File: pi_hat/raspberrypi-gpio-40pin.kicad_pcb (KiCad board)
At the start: 2 copper layers, 65 x 56 mm, 86 parts, among them J1 MC000052, J2 10pinIDC, J3 MOLEX_2031, P1 Conn_02x20_Odd_Even, Q1 IRLB8721PBF, SW1 SW_Push, U1 iCE40-HX4K-TQ144, U2 MCP1826S-3302E/DB, U3 MCP1826S-1202E/DB, U4 S25FL064LABMFI010, Y1 SIT8008BI-12-XXE-100

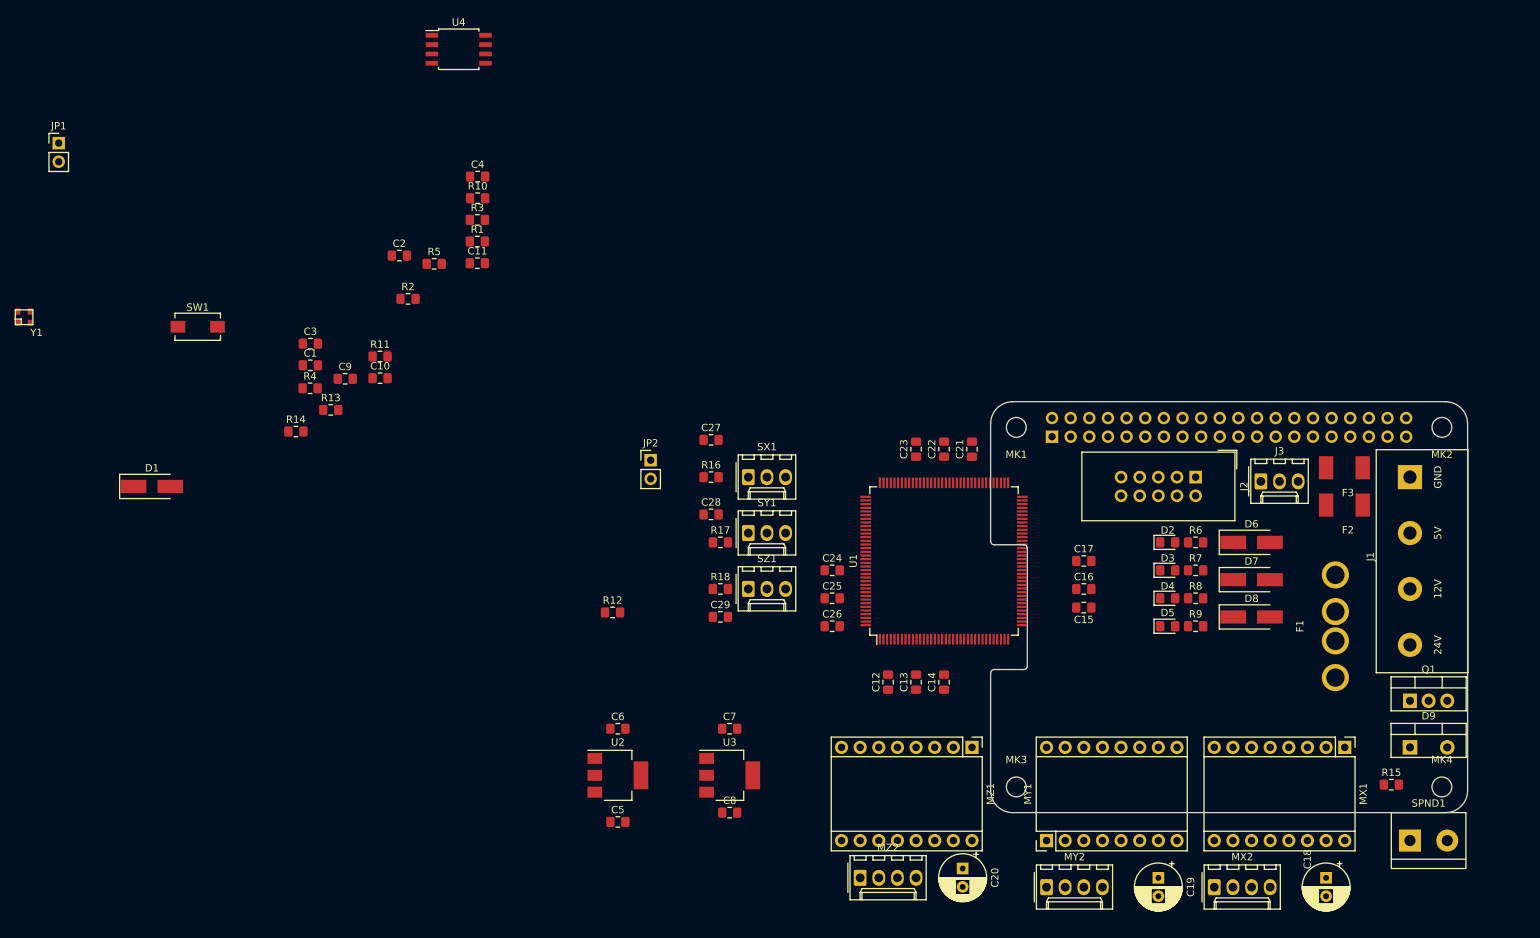
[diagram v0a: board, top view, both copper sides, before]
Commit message: reorganization of components
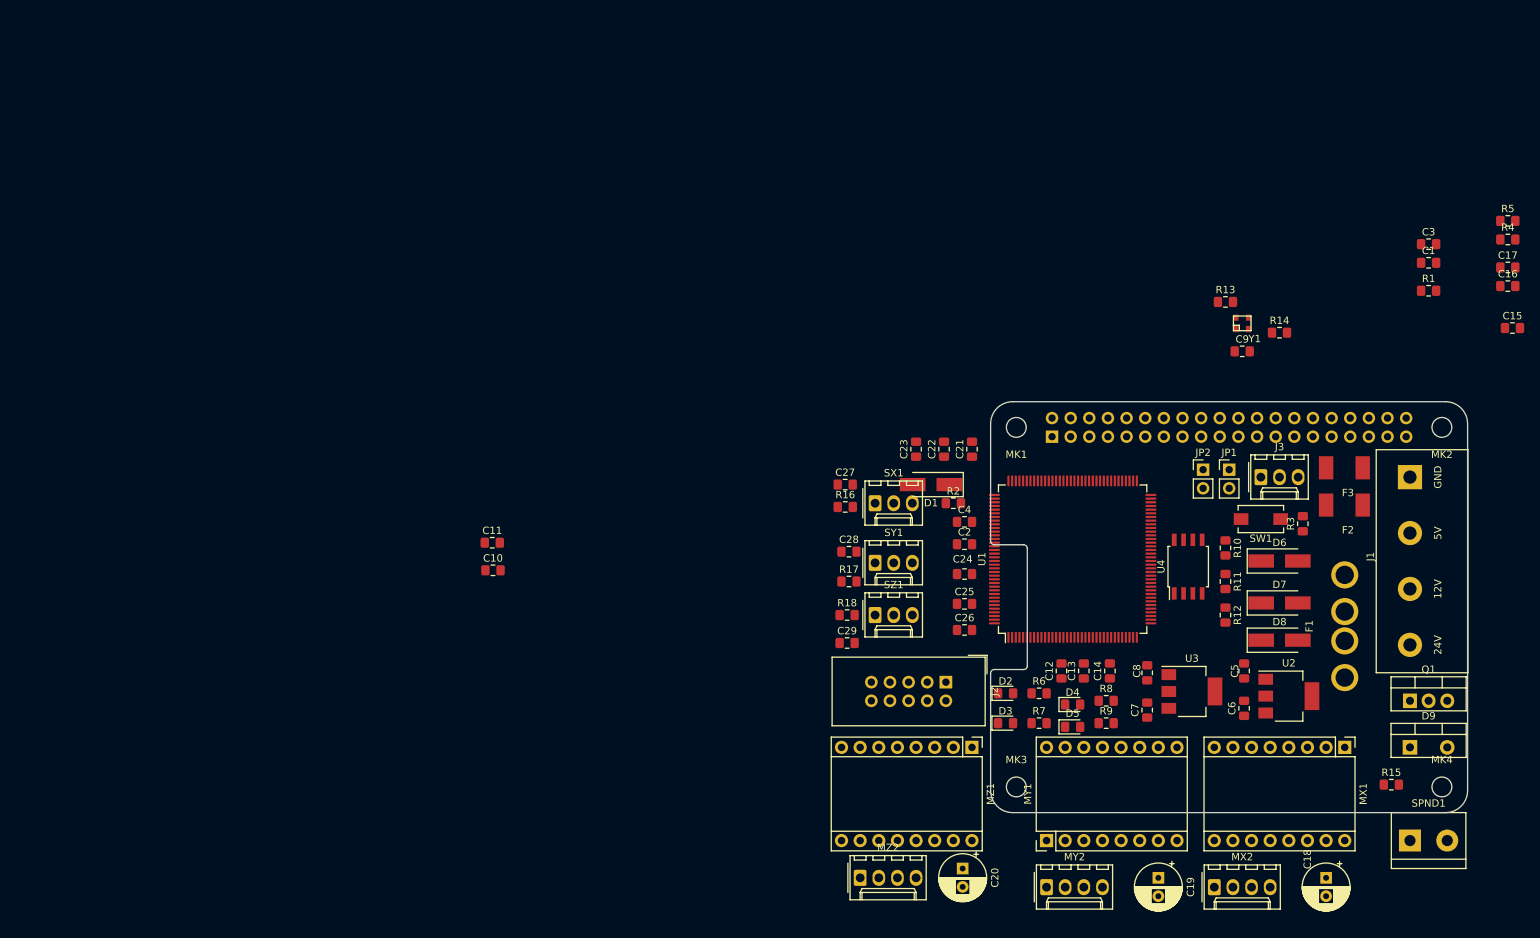
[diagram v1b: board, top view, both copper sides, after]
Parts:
- moved Y1 166.0 mm to (234.3, 83.3)
- moved JP1 165.6 mm to (232.5, 103.3)
- moved R4 164.5 mm to (270.5, 71.9)
- moved C1 153.0 mm to (259.7, 75.1)
- moved C3 153.0 mm to (259.7, 72.5)
- moved SW1 147.2 mm to (236.8, 110.0), turned to 180 degrees
- moved R5 146.4 mm to (270.5, 69.4)
- moved R14 134.7 mm to (239.4, 84.6)
- moved R1 129.8 mm to (259.7, 78.9)
- moved R13 122.8 mm to (232.0, 80.4)
- moved C9 122.3 mm to (234.3, 87.1)
- moved U4 121.9 mm to (226.9, 116.5), turned to 90 degrees
- moved R3 119.9 mm to (242.5, 110.6), turned to 90 degrees
- moved R11 119.2 mm to (232.0, 118.5), turned to 270 degrees
- moved R10 112.5 mm to (232.0, 113.9), turned to 270 degrees
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
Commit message: proceeded with routing
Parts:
- moved C11 93.5 mm to (225.4, 107.8)
- moved C10 85.4 mm to (216.3, 101.7)
- moved C3 62.3 mm to (227.9, 126.1), turned to 90 degrees
- moved R5 60.4 mm to (219.8, 102.2), turned to 90 degrees
- moved C1 59.0 mm to (231.0, 126.6), turned to 90 degrees
- moved R1 54.2 mm to (234.0, 126.6), turned to 90 degrees
- moved R4 52.7 mm to (231.5, 107.3), turned to 90 degrees
- moved C9 43.3 mm to (223.7, 129.2)
- moved C26 41.2 mm to (237.6, 126.1)
- moved R14 38.9 mm to (225.9, 121.0), turned to 90 degrees
- moved Y1 38.5 mm to (230.0, 121.6), turned to 90 degrees
- moved R13 30.7 mm to (228.5, 110.9)
- moved D8 23.7 mm to (249.0, 104.9), turned to 270 degrees
- moved MX1 21.4 mm to (230.9, 153.8), turned to 90 degrees
- moved MZ1 21.1 mm to (180.0, 153.0), turned to 90 degrees
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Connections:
- C18 pad 2: Net-(C18-Pad2) -> +24V
- MX1 pad 16: Net-(C18-Pad2) -> +24V
- U1 pad 37: POLY_EN -> SPINDLE_PWM
- U1 pad 62: SPINDLE_PWM -> POLY_EN
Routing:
- net GND: track 0.00 -> 234.2 mm
- net +24V: track 0.00 -> 182.9 mm
- net SPI1_MISO: track 0.00 -> 131.8 mm
- net SPI1_SCL: track 0.00 -> 120.6 mm
- net SPI1_CE: track 0.00 -> 100.5 mm
- net +3V3: track 0.00 -> 99.8 mm
- net ENABLE: track 0.00 -> 55.5 mm
- net SPI1_MOSI: track 0.00 -> 54.8 mm
- net +5V: track 0.00 -> 48.8 mm
- net SPINDLE_PWM: track 0.00 -> 43.5 mm
- net SPI1_YOZI: track 0.00 -> 22.6 mm
- net Net-(F1-Pad1): track 0.00 -> 21.6 mm
- net Net-(D9-Pad2): track 0.00 -> 21.5 mm
- net +1V2: track 0.00 -> 18.4 mm
- net Net-(F3-Pad2): track 0.00 -> 16.2 mm
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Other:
- board size 65 x 56 mm -> 86.8 x 69.4 mm
- net class Default: trace_width 0.2 -> 0.25; via_dia 0.9 -> 0.6; via_drill 0.6 -> 0.4
- net class Power removed
- rule trace_min: 0.1524 -> 0.2
- rule via_min_drill: 0.5 -> 0.3
- rule via_min_size: 0.8 -> 0.4

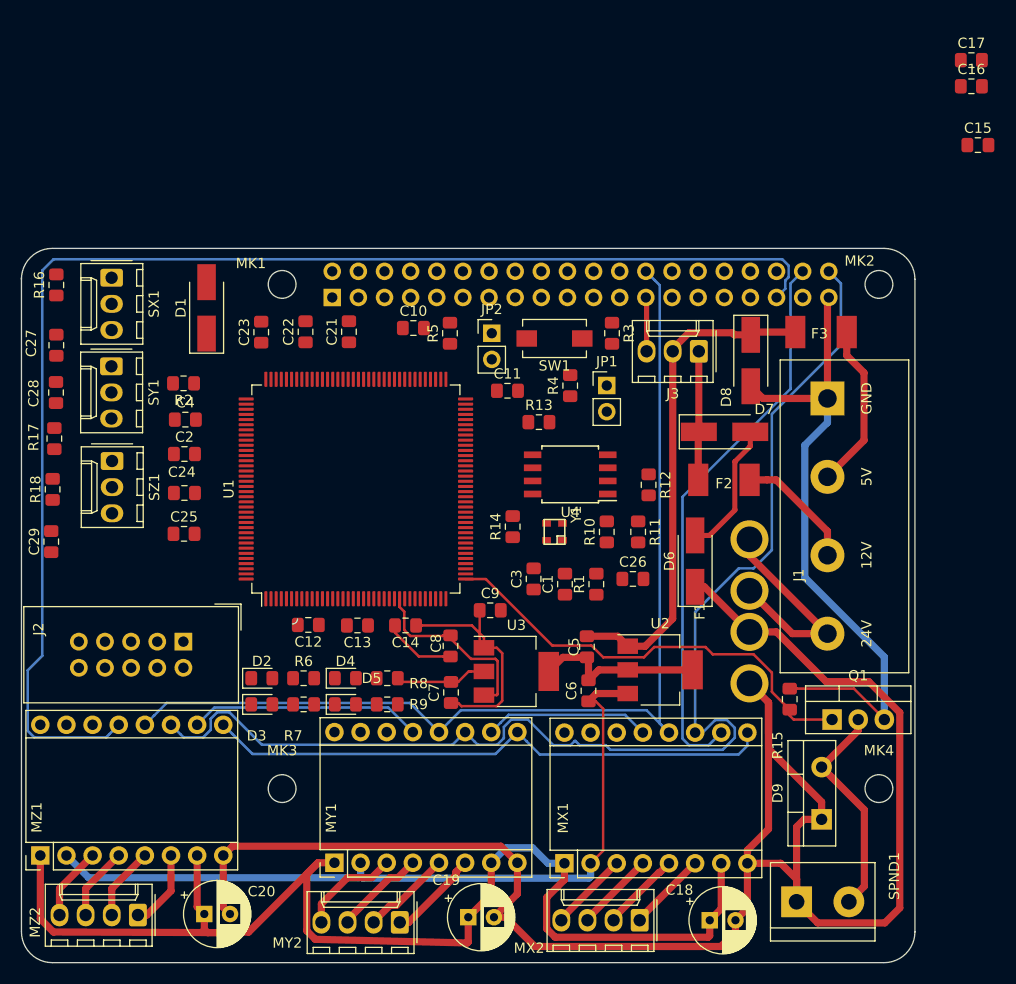
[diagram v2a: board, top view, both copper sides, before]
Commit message: continued routing, 3V and GND not fully connected
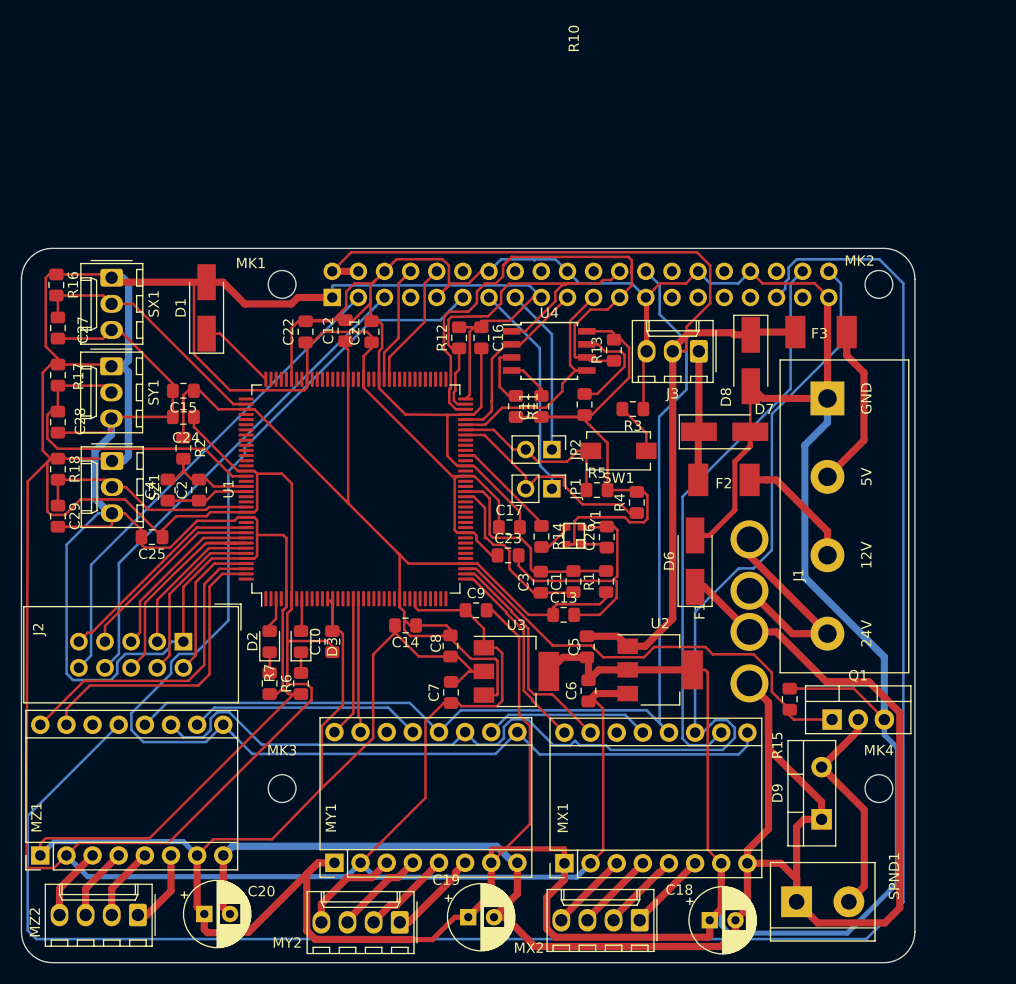
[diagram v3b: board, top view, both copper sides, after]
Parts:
- removed D4, D5: BLUE, LED_SMD:LED_0805_2012Metric_Pad1.15x1.40mm_HandSolder
- removed R8, R9: 240, Resistor_SMD:R_0805_2012Metric_Pad1.15x1.40mm_HandSolder
- moved C15 80.8 mm to (193.9, 107.8), turned to 180 degrees
- moved C17 63.9 mm to (225.6, 121.1)
- moved C16 53.5 mm to (222.9, 102.7), turned to 270 degrees
- moved C23 32.4 mm to (225.5, 123.8), turned to 0 degrees
- moved C10 31.5 mm to (208.4, 132.2), turned to 90 degrees
- moved C12 28.8 mm to (209.7, 102.0), turned to 90 degrees
- moved R12 23.3 mm to (220.7, 102.7), turned to 90 degrees
- moved R5 20.9 mm to (234.1, 117.5), turned to 0 degrees
- moved C13 20.1 mm to (230.9, 129.6), turned to 0 degrees
- moved R11 17.0 mm to (226.2, 109.4)
- moved R4 13.1 mm to (238.0, 118.7)
- moved JP2 12.7 mm to (229.7, 113.6), turned to 270 degrees
- moved SW1 12.6 mm to (236.2, 113.7)
- moved R10 12.6 mm to (232.9, 109.2), turned to 270 degrees
- moved U4 12.2 mm to (229.5, 104.0), turned to 0 degrees
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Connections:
- C12 pad 1: +3V3 -> +1V2
- C13 pad 1: +3V3 -> +1V2
- C14 pad 1: +3V3 -> +1V2
- C15 pad 1: +3V3 -> +1V2
- U1 pad 1: GPIO14 -> Net-(U1-Pad1)
- U1 pad 110: Net-(U1-Pad110) -> X_PO
- U1 pad 124: Net-(U1-Pad124) -> Y_PO
- U1 pad 130: Net-(U1-Pad130) -> Z_PO
- U1 pad 134: Net-(U1-Pad134) -> IC_HB_PWM1
- U1 pad 135: Net-(U1-Pad135) -> IC_HB_PWM2
- U1 pad 136: Net-(U1-Pad136) -> FAN_PWM
- U1 pad 137: Net-(U1-Pad137) -> PH_DIODE
- U1 pad 138: Net-(U1-Pad138) -> POLY_READY
- U1 pad 139: Net-(U1-Pad139) -> POLY_PWM
- U1 pad 141: Net-(U1-Pad141) -> POLY_EN
- U1 pad 142: Net-(U1-Pad142) -> Z_DIR
- U1 pad 143: Net-(U1-Pad143) -> Z_STEP
- U1 pad 18: Net-(U1-Pad18) -> Y_DIR
- U1 pad 19: Net-(U1-Pad19) -> Y_STEP
- U1 pad 2: GPIO15 -> Net-(U1-Pad2)
- U1 pad 28: USER_LED0 -> Net-(U1-Pad28)
- U1 pad 29: USER_LED1 -> Net-(U1-Pad29)
- U1 pad 3: Net-(U1-Pad3) -> USER_LED3
- U1 pad 31: USER_LED2 -> Net-(U1-Pad31)
- U1 pad 32: USER_LED3 -> Net-(U1-Pad32)
- U1 pad 37: SPINDLE_PWM -> X_DIR
- U1 pad 38: POLY_READY -> X_STEP
- U1 pad 39: POLY_PWM -> SPINDLE_PWM
- U1 pad 41: FAN_PWM -> Net-(U1-Pad41)
- U1 pad 42: PH_DIODE -> Net-(U1-Pad42)
- U1 pad 43: IC_HB_PWM2 -> Net-(U1-Pad43)
- U1 pad 44: IC_HB_PWM1 -> Net-(U1-Pad44)
- U1 pad 45: X_STEP -> Net-(U1-Pad45)
- U1 pad 47: X_DIR -> Net-(U1-Pad47)
- U1 pad 48: Y_STEP -> Net-(U1-Pad48)
- U1 pad 49: Y_DIR -> Net-(U1-Pad49)
- U1 pad 52: Z_STEP -> Net-(U1-Pad52)
- U1 pad 55: Z_DIR -> Net-(U1-Pad55)
- U1 pad 56: X_PO -> Net-(U1-Pad56)
- U1 pad 60: Y_PO -> Net-(U1-Pad60)
- U1 pad 62: POLY_EN -> Net-(U1-Pad62)
- U1 pad 63: Z_PO -> Net-(U1-Pad63)
- U1 pad 8: Net-(U1-Pad8) -> USER_LED2
- U1 pad 84: Net-(U1-Pad84) -> GPIO15
- U1 pad 85: Net-(U1-Pad85) -> GPIO14
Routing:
- net GND: track 234.2 -> 701.4 mm
- net +3V3: track 99.8 -> 511.4 mm
- net +1V2: track 18.4 -> 100.3 mm
- net ENABLE: track 55.5 -> 125.8 mm
- net SPI1_MISO: track 131.8 -> 186.6 mm
- net +5V: track 48.8 -> 99.9 mm
- net SPI0_SCL: track 0.00 -> 50.9 mm
- net POT_SDA: track 0.00 -> 47.2 mm
- net POT_SCL: track 0.00 -> 47.2 mm
- net SPI0_CE: track 0.00 -> 38.9 mm
- net Y_PO: track 0.00 -> 32.3 mm
- net Z_DIR: track 0.00 -> 30.9 mm
- net Z_STEP: track 0.00 -> 29.4 mm
- net X_PO: track 0.00 -> 25.0 mm
- net PH_DIODE: track 0.00 -> 24.1 mm
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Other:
- outline, holes or cut-outs redrawn
- board text removed: "DISPLAY"

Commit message: finished routing
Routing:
- net +5V: track 99.9 -> 160.0 mm, vias 0 -> 1
- net RP_CRESET: track 16.9 -> 28.1 mm
- net GND: track 701.4 -> 709.8 mm, vias 0 -> 6
- net +3V3: track 511.4 -> 504.8 mm, vias 0 -> 2
- net SPI1_MISO: track 186.6 -> 188.5 mm
- net +24V: track 182.9 -> 184.7 mm
- net SPI1_SCL: track 120.6 -> 118.8 mm
- net Net-(D9-Pad2): track 21.5 -> 20.3 mm
- added copper zone on B.Cu, net +24V
- added copper zone on B.Cu, net GND
- added copper zone on F.Cu, net GND

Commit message: finished routing
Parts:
- added G1: hexastorm, footprints:hexastorm, F.Cu at (228.6, 147.3)
- moved C25 2.79 mm to (188.4, 123.5)
- moved SX1 0.70 mm to (186.9, 96.2)
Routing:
- net +3V3: track 504.8 -> 528.0 mm
- net X_PO: track 25.0 -> 30.7 mm
- net GND: track 709.8 -> 713.4 mm
- net +1V2: track 100.3 -> 101.2 mm
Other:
- board size 86.8 x 69.4 mm -> 86.8 x 70.1 mm
